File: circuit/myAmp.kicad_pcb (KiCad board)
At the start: 2 copper layers, 48 parts, among them J1 JACK_MONO, J2 HOLE, J3 HOLE, J4 HOLE, J5 HOLE, Q1 J201, Q2 J201, U1 TPA3136D2

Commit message: small changes
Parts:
- moved R5 115.6 mm to (161.3, 78.4), turned to 90 degrees
- moved J1 93.3 mm to (139.7, 80.0)
- moved D3 87.7 mm to (157.5, 77.5), turned to 90 degrees
- moved D2 83.7 mm to (153.7, 77.5), turned to 90 degrees
- moved Q1 74.9 mm to (167.6, 76.2), turned to 90 degrees

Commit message: very rough layout
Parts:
- moved J2 100.9 mm to (146.7, 146.7)
- moved J5 87.3 mm to (146.7, 53.3)
- moved D4 81.0 mm to (90.8, 118.1)
- moved R5 80.9 mm to (82.5, 59.7)
- moved D2 80.7 mm to (74.9, 59.7)
- moved D3 80.7 mm to (78.7, 59.7)
- moved Q1 80.5 mm to (88.9, 59.7)
- moved J1 78.8 mm to (61.6, 69.8), turned to 90 degrees
- moved C15 75.5 mm to (55.9, 90.8), turned to 180 degrees
- moved RV4 74.3 mm to (121.9, 59.7), turned to 90 degrees
- moved D1 68.9 mm to (65.4, 120.7)
- moved RV2 67.3 mm to (104.8, 114.3)
- moved R3 66.1 mm to (74.9, 120.7), turned to 180 degrees
- moved R10 62.7 mm to (87.0, 123.2), turned to 90 degrees
- moved RV3 62.6 mm to (121.9, 80.0), turned to 90 degrees
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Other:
- board outline added: 100 x 100 mm

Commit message: more layout
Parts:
- removed R1, R2: 6K8, myAmp:R_10MM
- removed R6, R8: 2K2, myAmp:R_10MM
- added RV5: 50K, myAmp:RPOT_RKT6V, F.Cu at (92.7, 55.9)
- added RV6: 50K, myAmp:RPOT_RKT6V, F.Cu at (79.4, 70.5)
- added RV7: 5K, myAmp:RPOT_RKT6V, F.Cu at (79.4, 55.9)
- added RV8: 50K, myAmp:RPOT_RKT6V, F.Cu at (92.7, 70.5)
- Q1, Q2: footprint myAmp:J201 -> myAmp:SOT-23
- moved J2 45.0 mm to (112.0, 118.0)
- moved J5 34.7 mm to (112.0, 54.0)
- moved Q2 30.1 mm to (86.4, 67.9), turned to 180 degrees
- moved J3 26.1 mm to (54.0, 118.0)
- moved C10 23.6 mm to (102.2, 56.5)
- moved C11 23.6 mm to (99.1, 56.5)
- moved D4 22.3 mm to (68.6, 116.2), turned to 180 degrees
- moved C6 21.1 mm to (99.1, 85.7)
- moved R7 19.7 mm to (96.5, 82.5), turned to 90 degrees
- moved C4 19.0 mm to (94.6, 74.3), turned to 180 degrees
- moved D3 14.9 mm to (66.0, 52.0), turned to 0 degrees
- moved R9 13.9 mm to (78.7, 114.9), turned to 0 degrees
- moved R3 13.5 mm to (65.4, 111.1)
- moved RV4 13.4 mm to (110.5, 66.7)
- moved RV3 12.8 mm to (110.5, 85.7)
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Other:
- board size 100 x 100 mm -> 66 x 72 mm

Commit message: small changes
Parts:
- added BT1: Battery, myAmp:BATTERY, F.Cu at (87.6, 79.4)
- RV7: value 5K -> 2K
- moved C6 5.85 mm to (100.3, 91.4), turned to 270 degrees
- moved R7 3.86 mm to (100.3, 81.9)
- turned C5 to 0 degrees
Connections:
- net Net-(C4-Pad2) renamed /TONE_IN
- net Net-(C6-Pad1) renamed /TONE_OUT
- J2 pad 1: (no net) -> Net-(J2-Pad1)
- J3 pad 1: (no net) -> Net-(J3-Pad1)
- J4 pad 1: (no net) -> Net-(J4-Pad1)
- J5 pad 1: (no net) -> Net-(J5-Pad1)
- U1 pad 13: (no net) -> Net-(U1-Pad13)
- U1 pad 3: (no net) -> Net-(U1-Pad3)
- U1 pad 4: (no net) -> Net-(U1-Pad4)
- U1 pad 5: (no net) -> Net-(U1-Pad5)
- U1 pad 6: (no net) -> Net-(U1-Pad6)
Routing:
- added copper zone on B.Cu, net GND

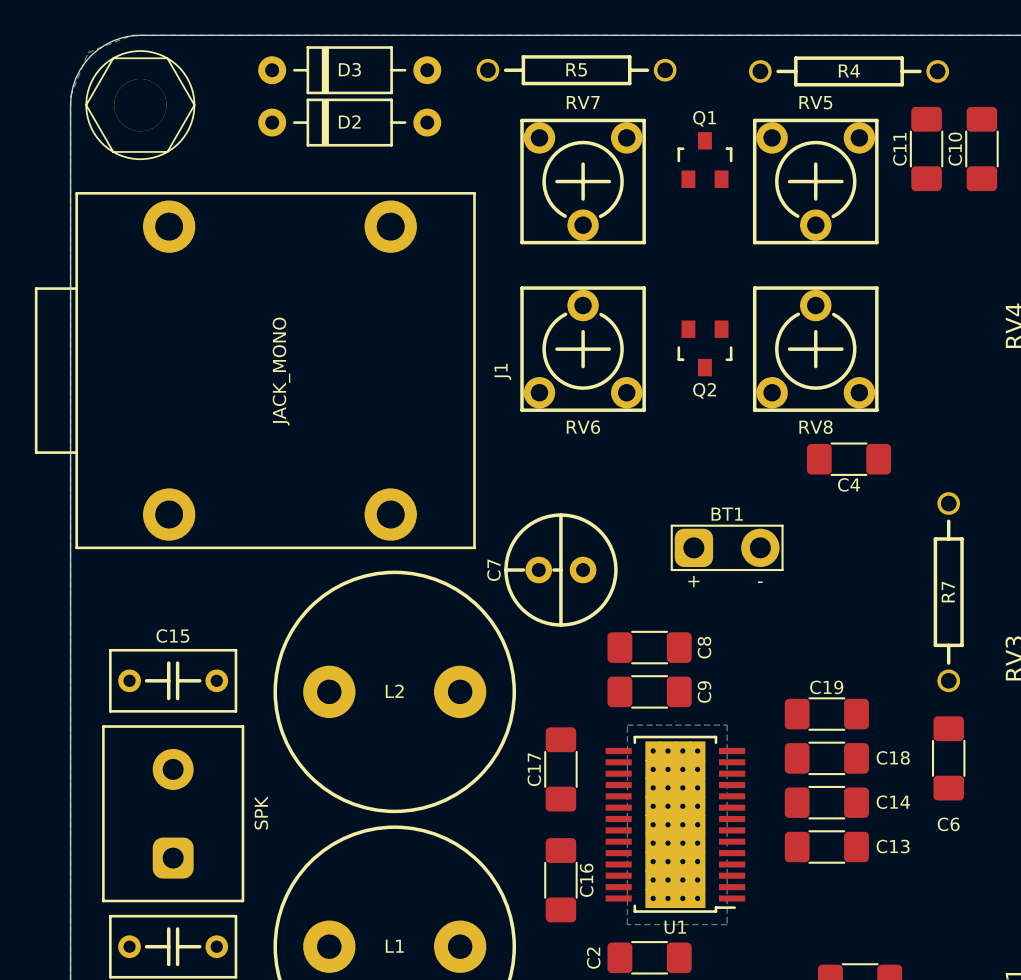
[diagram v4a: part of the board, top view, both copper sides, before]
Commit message: some 3D model references corrected
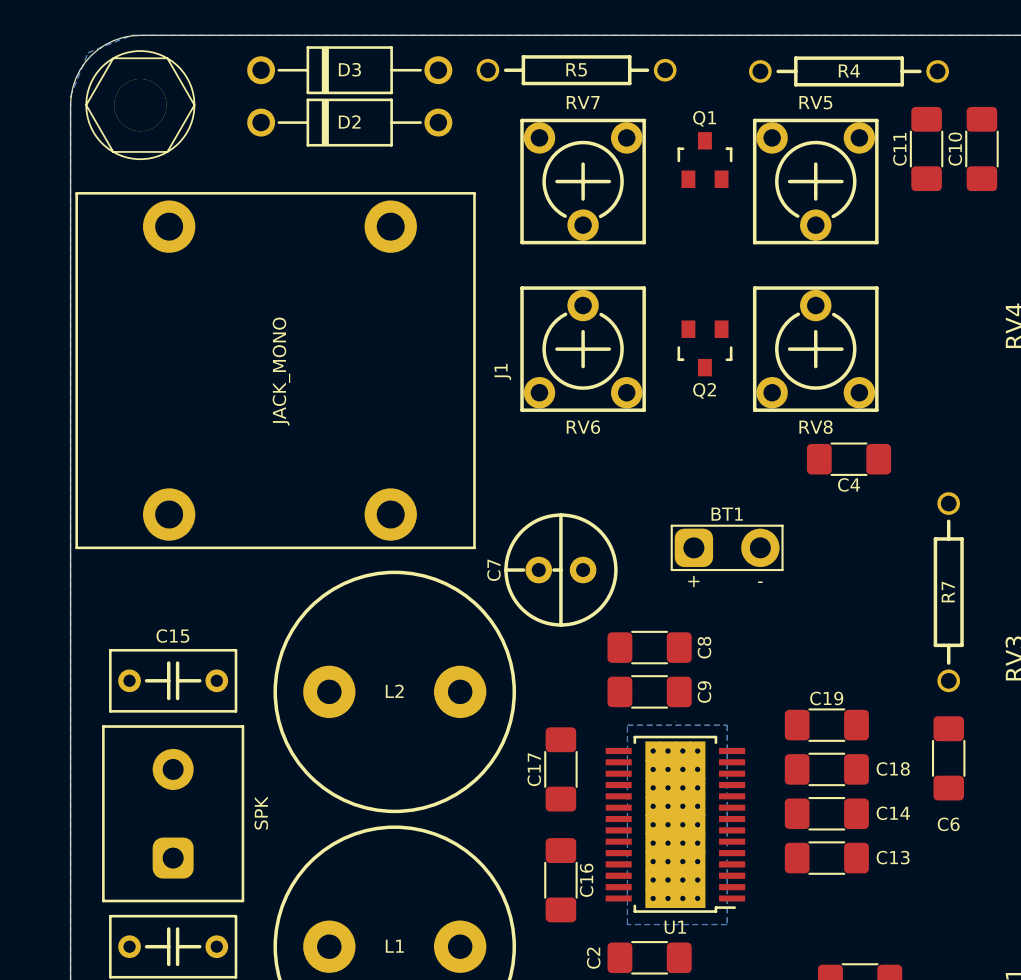
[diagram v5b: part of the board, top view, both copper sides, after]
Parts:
- moved C13 0.64 mm to (93.3, 97.2)
- moved C18 0.64 mm to (93.3, 92.1)
- moved C14 0.63 mm to (93.3, 94.6)
- moved C19 0.63 mm to (93.3, 89.5)

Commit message: trace widths
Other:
- net class Default: clearance 0.2 -> 0.2032; trace_width 0.25 -> 0.2032
- rule trace_clearance: 0.2 -> 0.2032
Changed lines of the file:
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@@
   )
   (setup
-    (last_trace_width 0.25)
-    (trace_clearance 0.2)
+    (last_trace_width 0.2032)
+    (user_trace_width 0.254)
+    (user_trace_width 0.3048)
+    (user_trace_width 0.3556)
+    (user_trace_width 0.4064)
+    (trace_clearance 0.2032)
     (zone_clearance 0.508)
     (zone_45_only no)
@@
   (net 39 /TONE_OUT)
   (net_class Default "This is the default net class."
-    (clearance 0.2)
-    (trace_width 0.25)
+    (clearance 0.2032)
+    (trace_width 0.2032)
     (via_dia 0.8)
     (via_drill 0.4)

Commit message: started routing
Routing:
- net VDD: track 0.00 -> 60.4 mm
- net Net-(C5-Pad2): track 0.00 -> 54.4 mm
- net Net-(D2-Pad2): track 0.00 -> 37.1 mm
- net Net-(C10-Pad1): track 0.00 -> 36.5 mm
- net /TONE_IN: track 0.00 -> 28.4 mm
- net /TONE_OUT: track 0.00 -> 26.5 mm
- net PREAMP_OUT: track 0.00 -> 26.3 mm
- net /SD_FAULT: track 0.00 -> 20.4 mm
- net Net-(C6-Pad2): track 0.00 -> 16.6 mm
- net Net-(C11-Pad1): track 0.00 -> 15.4 mm
- net /OUTR: track 0.00 -> 14.9 mm
- net /OUTL: track 0.00 -> 14.4 mm
- net Net-(C5-Pad1): track 0.00 -> 14.1 mm
- net Net-(C15-Pad1): track 0.00 -> 13.5 mm
- net GND: track 0.00 -> 13.1 mm, vias 0 -> 1
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
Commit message: routing mostly done
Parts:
- moved BT1 39.7 mm to (78.7, 118.1)
- moved R9 2.54 mm to (78.7, 112.4)
- moved R10 2.54 mm to (78.7, 114.9)
- moved C1 2.01 mm to (78.1, 107.3)
- moved C2 1.27 mm to (84.5, 102.9)
- moved C3 1.27 mm to (84.5, 105.4)
- moved C8 1.27 mm to (84.5, 85.1)
- moved C9 1.27 mm to (84.5, 87.6)
- moved C16 0.89 mm to (78.1, 99.3)
- moved C17 0.89 mm to (78.1, 91.2)
- moved C6 0.64 mm to (101.0, 91.4)
- moved R7 0.64 mm to (101.0, 81.9)
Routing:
- net VDD: track 60.4 -> 177.7 mm, vias 0 -> 1
- net Net-(C4-Pad1): track 0.00 -> 46.1 mm
- net GND: track 13.1 -> 28.8 mm, vias 1 -> 2
- net Net-(C17-Pad2): track 4.22 -> 10.6 mm, vias 0 -> 2
- net Net-(C16-Pad2): track 4.54 -> 10.8 mm, vias 0 -> 2
- net Net-(C5-Pad2): track 54.4 -> 55.9 mm
- net /SD_FAULT: track 20.4 -> 18.9 mm
- net PREAMP_OUT: track 26.3 -> 27.1 mm
- net /TONE_IN: track 28.4 -> 29.1 mm
- net /OUTL: track 14.4 -> 13.8 mm
- net /GVDD: track 3.87 -> 4.52 mm
- net Net-(C6-Pad2): track 16.6 -> 16.0 mm
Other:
- board text added: "Bass"
- board text added: "Middle"
- board text added: "Treble"
- board text added: "Volume"
